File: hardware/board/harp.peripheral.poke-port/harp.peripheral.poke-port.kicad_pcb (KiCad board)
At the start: 2 copper layers, 26.3 x 26.3 mm, 24 parts, among them J1 Conn_01x03_Socket, U1 TPS63060, U2 EE-SX1140, U3 74LVCH2T45DC

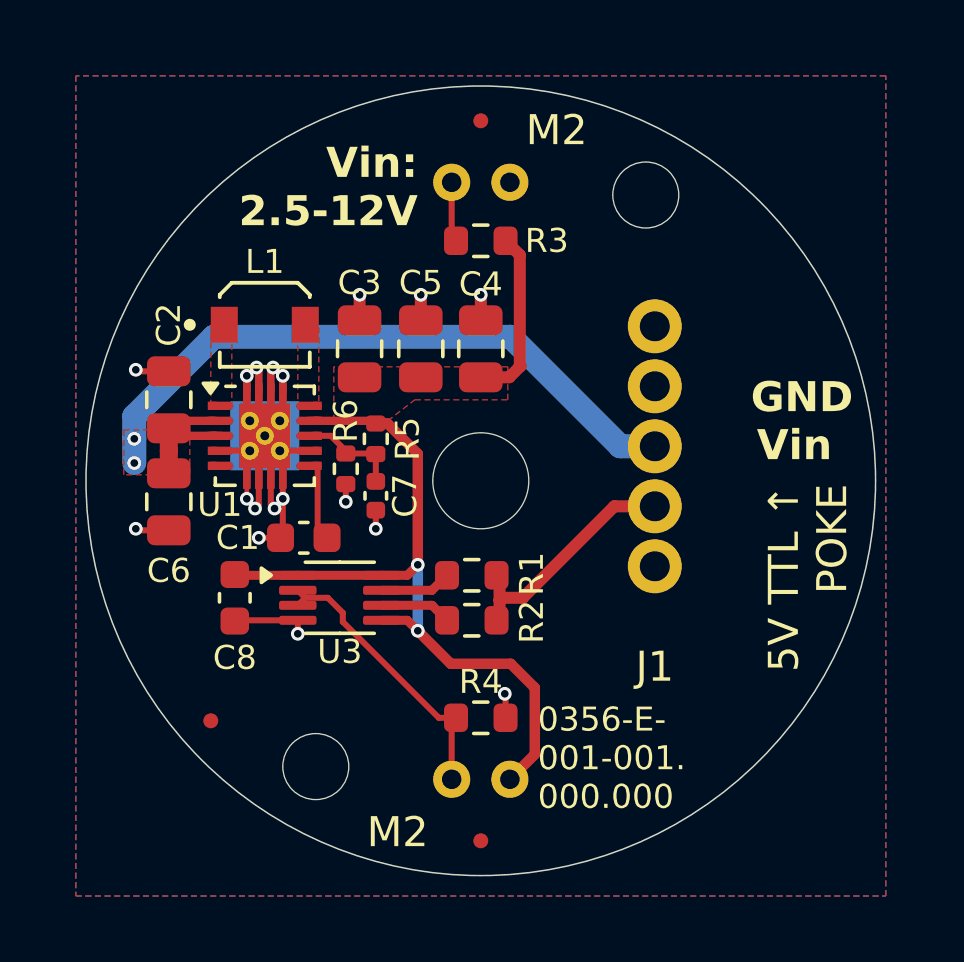
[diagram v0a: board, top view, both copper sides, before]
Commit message: Vacuum port option
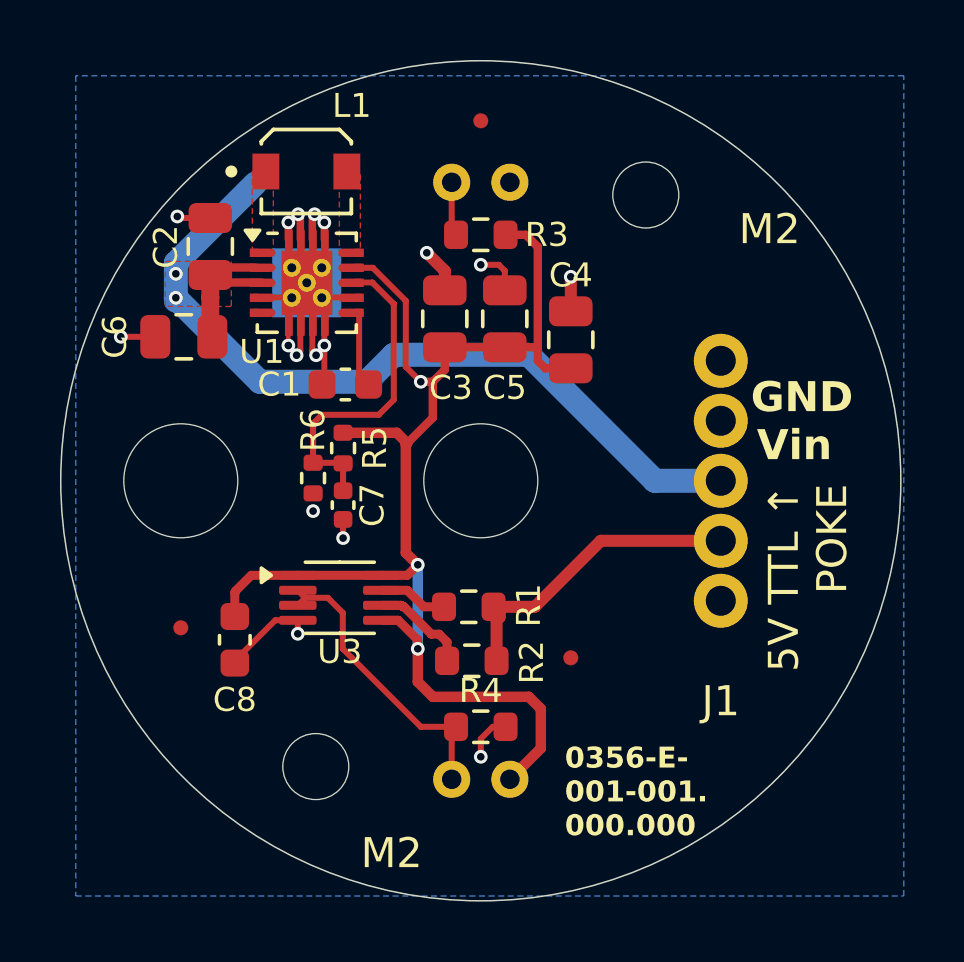
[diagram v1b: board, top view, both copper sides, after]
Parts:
- added REF**: MountingHole_3.7mm, MountingHole:MountingHole_3.7mm, F.Cu at (140.0, 100.0)
- moved REF** 6.80 mm to (153.0, 105.9)
- moved C6 5.52 mm to (140.1, 95.2), turned to 180 degrees
- moved C1 5.29 mm to (145.5, 96.8)
- moved C2 5.29 mm to (141.0, 92.2)
- moved L1 5.29 mm to (144.2, 89.7)
- moved U1 5.29 mm to (144.2, 93.4)
- moved REF** 3.26 mm to (140.0, 104.9)
- moved C4 3.01 mm to (153.0, 95.3)
- moved C3 3.01 mm to (148.8, 94.6)
- moved C5 2.97 mm to (150.8, 94.6)
- moved J1 2.48 mm to (158.0, 100.0)
- moved C8 1.40 mm to (141.8, 105.3)
- moved R2 1.35 mm to (149.7, 106.0)
- moved C7 1.13 mm to (145.4, 100.8)
- moved R5 1.13 mm to (145.4, 98.9)
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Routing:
- net +5V: track 31.5 -> 45.1 mm, vias 2 -> 3
- net Net-(U1-FB): track 3.44 -> 11.2 mm
- net VPP: track 26.4 -> 31.3 mm
- net /TTL_POKE: track 8.05 -> 10.4 mm
- net GND: track 20.1 -> 21.9 mm, vias 18 -> 17
- net Net-(U3-2B): track 2.38 -> 3.31 mm
- removed copper zone on F.Cu, net +5V
- removed copper zone on F.Cu, net GND
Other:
- board size 26.3 x 26.3 mm -> 28 x 28 mm

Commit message: Fab files for vacuum port
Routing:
- added copper zone on F.Cu, net GND
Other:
- board text added: "2.5-12Vin"
- board text added: "5V TTL ←Poke"
- board text added: "S Vasquez & N Mars Mar 4 2026"
- board text removed: "5V TTL ↑ POKE"
- board text removed: "Sonya Vasquez Feb 3, 2025"
- board text removed: "Vin: 2.5-12V"
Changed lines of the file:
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@@
 			(drillshape 0)
 			(scaleselection 1)
-			(outputdirectory "exports/gerbers/")
+			(outputdirectory "fab_files/")
 		)
 	)
@@
 		(tags "capacitor")
 		(property "Reference" "C4"
-			(at -2.15 0 180)
+			(at 2.3 0 180)
 			(layer "F.SilkS")
 			(effects
@@
 		)
 		(embedded_fonts no)
-		(model "${KICAD8_3DMODEL_DIR}/Package_SON.3dshapes/Texas_S-PWSON-N10.wrl"
+		(model "${KIPRJMOD}/3d Models/Texas_TPS63060DSCR.step"
 			(offset
 				(xyz 0 0 0)
@@
 			)
 			(rotate
-				(xyz 0 0 0)
+				(xyz -90 -0 -0)
 			)
 		)
@@
 			(layer "F.CrtYd")
 		)
-		(fp_text user "${REFERENCE}"
-			(at 0 0 0)
-			(layer "F.Fab")
-			(effects
-				(font
-					(size 1 1)
-					(thickness 0.15)
-				)
-			)
-		)
 		(pad "" np_thru_hole circle
 			(at 0 0)
-			(size 3.7 3.7)
+			(size 2.8 2.8)
 			(drill 3.8)
 			(layers "*.Cu" "*.Mask")
@@
 		(tags "resistor")
 		(property "Reference" "R4"
-			(at 0 -1.2 0)
+			(at 2.3 0 0)
 			(layer "F.SilkS")
 			(effects
@@
 		(tags "capacitor")
 		(property "Reference" "C6"
-			(at 2.3 0 90)
+			(at 2.1 0 90)
 			(layer "F.SilkS")
 			(effects
@@
 		(at 144.185 89.69)
 		(property "Reference" "L1"
-			(at 1.515 -2.19 0)
+			(at 1.815 -2.19 0)
 			(layer "F.SilkS")
 			(effects
@@
 		)
 		(embedded_fonts no)
-		(model "/home/poofjunior/projects/kicad_libraries/kicad-lib/kicad-lib.3dshapes/L_Murata_1226AS-H-1R5N_P2.step"
+		(model "${KIPRJMOD}/3d Models/L_Murata_1226AS-H-1R5N_P2.step"
 			(offset
 				(xyz 0 0 0)
@@
 		)
 		(embedded_fonts no)
-		(model "/home/poofjunior/projects/kicad_libraries/kicad-lib/kicad-lib.3dshapes/3M_Mini-Clamp_37203-62B3-003 PL.stp"
+		(model "${KIPRJMOD}/3d Models/3M_MiniClamp_37203-62B3-003 PL step.stp"
 			(offset
 				(xyz -5.8 -21.85 -5.42)
@@
 		)
 		(embedded_fonts no)
-		(model "/home/poofjunior/projects/kicad_libraries/kicad-lib/kicad-lib.3dshapes/Omron_EE_SX1140.step"
+		(model "${KIPRJMOD}/3d Models/Omron_EE_SX1140.step"
 			(offset
 				(xyz -10 -1 -0.015)
@@
 		(layer "User.2")
 	)
-	(gr_text "GND"
-		(at 159 97.8 0)
+	(gr_text "2.5-12Vin"
+		(at 157.4 93.4 0)
 		(layer "F.SilkS")
 		(effects
@@
 				(bold yes)
 			)
-			(justify left bottom)
-		)
-	)
-	(gr_text "5V TTL ↑\nPOKE"
-		(at 162.3 100.1 90)
-		(layer "F.SilkS")
-		(effects
-			(font
-				(size 1 1)
-				(thickness 0.2)
-			)
-			(justify right bottom)
+			(justify bottom)
 		)
 	)
 	(gr_text "M2"
-		(at 146 113 0)
+		(at 145.6 111.6 0)
 		(layer "F.SilkS")
 		(effects
@@
 		)
 	)
-	(gr_text "Vin"
-		(at 159.2 99.4 0)
+	(gr_text "M2"
+		(at 152.8 89.2 0)
 		(layer "F.SilkS")
 		(effects
@@
 				(size 1 1)
 				(thickness 0.2)
-				(bold yes)
 			)
 			(justify left bottom)
 		)
 	)
-	(gr_text "M2"
-		(at 158.6 92.2 0)
-		(layer "F.SilkS")
+	(gr_text "S Vasquez & N Mars\nMar 4 2026"
+		(at 155.8 101.15 90)
+		(layer "B.SilkS")
 		(effects
 			(font
@@
 				(thickness 0.2)
 			)
-			(justify left bottom)
+			(justify bottom mirror)
 		)
 	)
-	(gr_text "Sonya Vasquez\nFeb 3, 2025"
-		(at 141.3 93.88 90)
+	(gr_text "5V TTL\n←Poke"
+		(at 159.4 101.6 180)
 		(layer "B.SilkS")
 		(effects
 			(font
-				(size 1 1)
-				(thickness 0.2)
+				(size 0.8 0.8)
+				(thickness 0.16)
+				(bold yes)
 			)
 			(justify left bottom mirror)
 		)
 	)
-	(gr_text "Vin:\n2.5-12V"
-		(at 156.6 101.1 90)
+	(gr_text "GND"
+		(at 159.6 98 180)
 		(layer "B.SilkS")
 		(effects
 			(font
-				(size 1 1)
-				(thickness 0.2)
+				(size 0.8 0.8)
+				(thickness 0.16)
 				(bold yes)
 			)
-			(justify right bottom mirror)
+			(justify left mirror)
 		)
 	)
@@
 		)
 	)
+	(gr_text "Vin"
+		(at 159.6 100 180)
+		(layer "B.SilkS")
+		(effects
+			(font
+				(size 0.8 0.8)
+				(thickness 0.16)
+				(bold yes)
+			)
+			(justify left mirror)
+		)
+	)
+	(segment
+		(start 141.3 89.9)
+		(end 141.3 90.925)
+		(width 0.2)
+		(layer "F.Cu")
+		(net 1)
+	)
 	(segment
 		(start 138 95.2)
@@
 	)
 	(segment
-		(start 140.985 91.24)
-		(end 139.935 91.24)
-		(width 0.2)
-		(layer "F.Cu")
-		(net 1)
-	)
-	(segment
 		(start 143.985 95.69)
 		(end 143.985 94.815)
@@
 	)
 	(segment
+		(start 141.3 90.925)
+		(end 140.985 91.24)
+		(width 0.2)
+		(layer "F.Cu")
+		(net 1)
+	)
+	(segment
 		(start 143.15 104.65)
 		(end 141.8 106)
@@
 	)
 	(segment
-		(start 139.935 91.24)
-		(end 139.885 91.19)
-		(width 0.2)
-		(layer "F.Cu")
-		(net 1)
-	)
-	(segment
 		(start 143.585 91.965)
 		(end 143.585 91.39)
@@
 	)
 	(via
-		(at 139.885 91.19)
+		(at 141.3 89.9)
 		(size 0.4572)
 		(drill 0.254)
@@
 		(min_thickness 0.25)
 		(filled_areas_thickness no)
-		(fill
+		(fill yes
 			(thermal_gap 0.5)
 			(thermal_bridge_width 0.5)
@@
 		(net 1)
 		(net_name "GND")
-		(layer "B.Cu")
+		(layers "F.Cu" "B.Cu")
 		(hatch edge 0.5)
 		(priority 1)
@@
 		(min_thickness 0.25)
 		(filled_areas_thickness no)
-		(fill
+		(fill yes
 			(thermal_gap 0.5)
 			(thermal_bridge_width 0.5)

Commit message: Fixed R4 -> 510ohm
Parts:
- R4: value 100 -> 510
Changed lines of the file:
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@@
 		)
 		(property ki_fp_filters "C_*")
-		(sheetname "Root")
+		(sheetname "/")
 		(sheetfile "harp.peripheral.poke-port.kicad_sch")
 		(attr smd)
@@
 		)
 		(property ki_fp_filters "C_*")
-		(sheetname "Root")
+		(sheetname "/")
 		(sheetfile "harp.peripheral.poke-port.kicad_sch")
 		(attr smd)
@@
 		)
 		(property ki_fp_filters "Texas*S*PWSON*N10*")
-		(sheetname "Root")
+		(sheetname "/")
 		(sheetfile "harp.peripheral.poke-port.kicad_sch")
 		(attr smd)
@@
 		)
 		(property ki_fp_filters "R_*")
-		(sheetname "Root")
+		(sheetname "/")
 		(sheetfile "harp.peripheral.poke-port.kicad_sch")
 		(attr smd)
@@
 		)
 		(property ki_fp_filters "R_*")
-		(sheetname "Root")
+		(sheetname "/")
 		(sheetfile "harp.peripheral.poke-port.kicad_sch")
 		(attr smd)
@@
 		)
 		(property ki_fp_filters "C_*")
-		(sheetname "Root")
+		(sheetname "/")
 		(sheetfile "harp.peripheral.poke-port.kicad_sch")
 		(attr smd)
@@
 			)
 		)
-		(property "Value" "100"
+		(property "Value" "510"
 			(at 0 1.43 0)
 			(layer "F.Fab")
@@
 			)
 		)
-		(property "Datasheet" "https://www.yageo.com/upload/media/product/productsearch/datasheet/rchip/PYu-SR_20105_RoHS_L_10.pdf"
+		(property "Datasheet" "https://www.koaspeer.com/pdfs/SG73P.pdf"
 			(at 0 0 0)
 			(unlocked yes)
@@
 			)
 		)
-		(property "Link" "https://www.digikey.com/en/products/detail/yageo/SR0603FR-7T100RL/9373096"
+		(property "Link" "https://www.digikey.com/en/products/detail/koa-speer-electronics-inc/SG73P1JTTD5100F/10188211"
 			(at 0 0 0)
 			(unlocked yes)
@@
 			)
 		)
-		(property "Manufacturer" "Yageo"
+		(property "Manufacturer" "KOA Speer Electronics, Inc."
 			(at 0 0 0)
 			(unlocked yes)
@@
 			)
 		)
-		(property "Manufacturer Number" "SR0603FR-7T100RL"
+		(property "Manufacturer Number" "SG73P1JTTD5100F"
 			(at 0 0 0)
 			(unlocked yes)
@@
 			)
 		)
-		(property "Notes" "1/4W"
+		(property "Notes" "1/3W"
 			(at 0 0 0)
 			(unlocked yes)
@@
 		)
 		(property ki_fp_filters "R_*")
-		(sheetname "Root")
+		(sheetname "/")
 		(sheetfile "harp.peripheral.poke-port.kicad_sch")
 		(attr smd)
@@
 		)
 		(property ki_fp_filters "R_*")
-		(sheetname "Root")
+		(sheetname "/")
 		(sheetfile "harp.peripheral.poke-port.kicad_sch")
 		(attr smd)
@@
 		)
 		(property ki_fp_filters "R_*")
-		(sheetname "Root")
+		(sheetname "/")
 		(sheetfile "harp.peripheral.poke-port.kicad_sch")
 		(attr smd)
@@
 		)
 		(property ki_fp_filters "C_*")
-		(sheetname "Root")
+		(sheetname "/")
 		(sheetfile "harp.peripheral.poke-port.kicad_sch")
 		(attr smd)
@@
 		)
 		(property ki_fp_filters "C_*")
-		(sheetname "Root")
+		(sheetname "/")
 		(sheetfile "harp.peripheral.poke-port.kicad_sch")
 		(attr smd)
@@
 		)
 		(property ki_fp_filters "C_*")
-		(sheetname "Root")
+		(sheetname "/")
 		(sheetfile "harp.peripheral.poke-port.kicad_sch")
 		(attr smd)
@@
 		)
 		(property ki_fp_filters "C_*")
-		(sheetname "Root")
+		(sheetname "/")
 		(sheetfile "harp.peripheral.poke-port.kicad_sch")
 		(attr smd)
@@
 		)
 		(property ki_fp_filters "Choke_* *Coil* Inductor_* L_*")
-		(sheetname "Root")
+		(sheetname "/")
 		(sheetfile "harp.peripheral.poke-port.kicad_sch")
 		(attr smd)
@@
 		)
 		(property ki_fp_filters "R_*")
-		(sheetname "Root")
+		(sheetname "/")
 		(sheetfile "harp.peripheral.poke-port.kicad_sch")
 		(attr smd)
@@
 		)
 		(property ki_fp_filters "C_*")
-		(sheetname "Root")
+		(sheetname "/")
 		(sheetfile "harp.peripheral.poke-port.kicad_sch")
 		(attr smd)
@@
 		)
 		(property ki_fp_filters "VSSOP*2.3x2mm*P0.5mm*")
-		(sheetname "Root")
+		(sheetname "/")
 		(sheetfile "harp.peripheral.poke-port.kicad_sch")
 		(attr smd)
@@
 		)
 		(property ki_fp_filters "Connector*:*_1x??_*")
-		(sheetname "Root")
+		(sheetname "/")
 		(sheetfile "harp.peripheral.poke-port.kicad_sch")
 		(attr through_hole)
@@
 		)
 		(property ki_fp_filters "*ITR9608*")
-		(sheetname "Root")
+		(sheetname "/")
 		(sheetfile "harp.peripheral.poke-port.kicad_sch")
 		(attr through_hole)
